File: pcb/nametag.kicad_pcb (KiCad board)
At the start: 2 copper layers, 80 x 55 mm, 34 parts, among them J1 Conn_01x04, SW1 TS02-66-43-BK-160-LCR-D, U2 AVR16DD20-I/SO, U3 TPS613226ADBVR

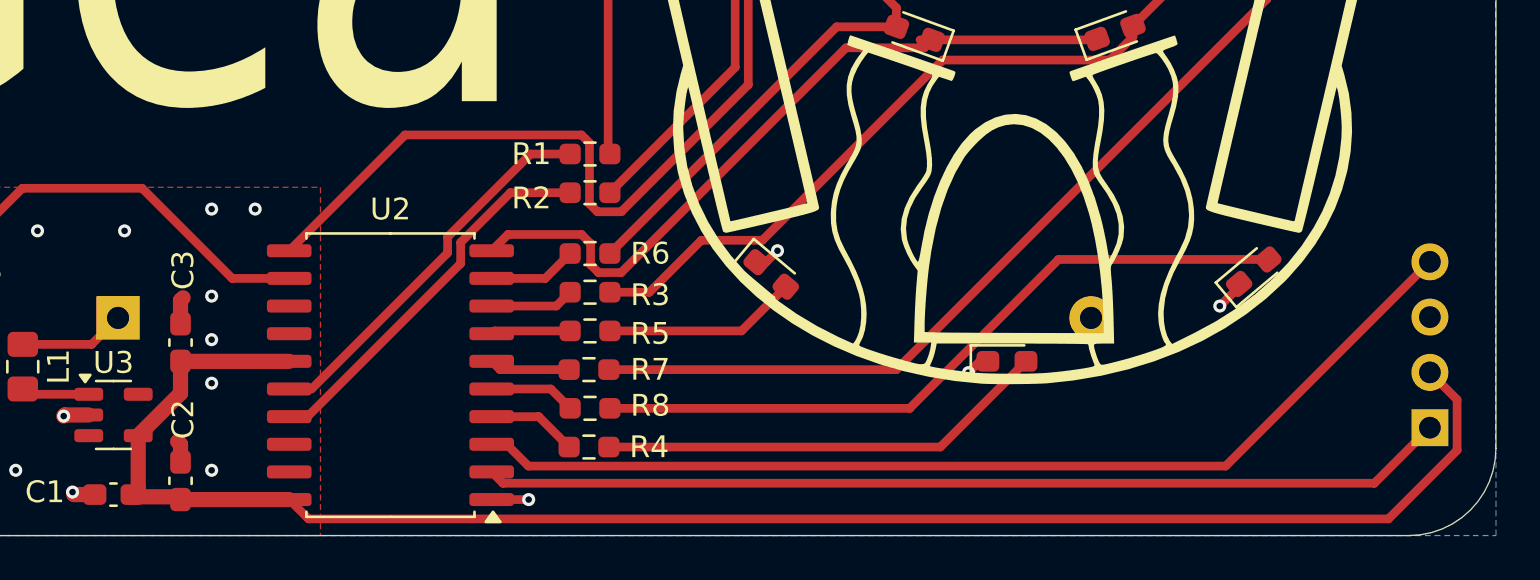
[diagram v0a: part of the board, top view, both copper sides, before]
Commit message: Swap to STC8H1K08 and work on JLCPCB assembly support
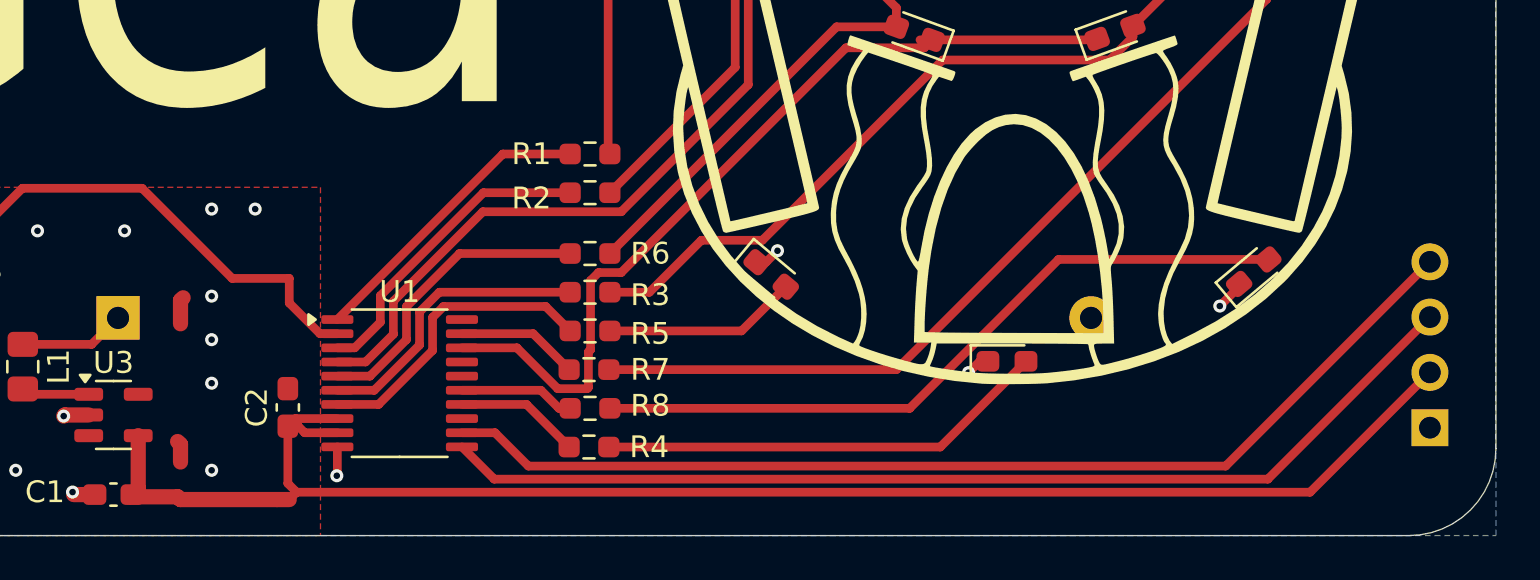
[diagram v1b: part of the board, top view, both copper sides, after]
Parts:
- removed C3: 0.1u, Capacitor_SMD:C_0603_1608Metric_Pad1.08x0.95mm_HandSolder
- removed U2: AVR16DD20-I/SO, Package_SO:SOIC-20W_7.5x12.8mm_P1.27mm
- added U1: ~, Package_SO:TSSOP-20_4.4x6.5mm_P0.65mm, F.Cu at (69.6, 88.0)
- C2: value 0.1u -> 100n
- moved C2 5.97 mm to (64.5, 89.1)
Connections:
- J1 pad 1: /Mcu/UPDI_RSTN -> GND
- J1 pad 3: GND -> /Mcu/UART_RX
- J1 pad 4: /Mcu/UPDI_PROG -> /Mcu/UART_TX
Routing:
- net /Mcu/UART_TX: track 0.00 -> 49.0 mm
- net /Mcu/UART_RX: track 0.00 -> 48.2 mm
- net /Mcu/UPDI_PROG: track 47.4 -> 0.00 mm
- net /Mcu/UPDI_RSTN: track 44.4 -> 0.00 mm
- net /Mcu/pwm3: track 3.66 -> 13.9 mm
- net /Mcu/pwm5: track 4.08 -> 13.9 mm
- net /Mcu/pwm4: track 3.87 -> 13.4 mm
- net +3.3V: track 79.0 -> 73.2 mm
- net /Mcu/cathode0: track 34.4 -> 40.0 mm
- net /Mcu/pwm6: track 17.8 -> 13.8 mm
- net /Mcu/switch: track 26.3 -> 30.3 mm
- net /Mcu/cathode1: track 61.5 -> 57.8 mm
- net /Mcu/pwm7: track 17.7 -> 14.4 mm
- net /Mcu/pwm2: track 3.72 -> 5.61 mm
- net /Mcu/pwm0: track 4.14 -> 5.73 mm
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
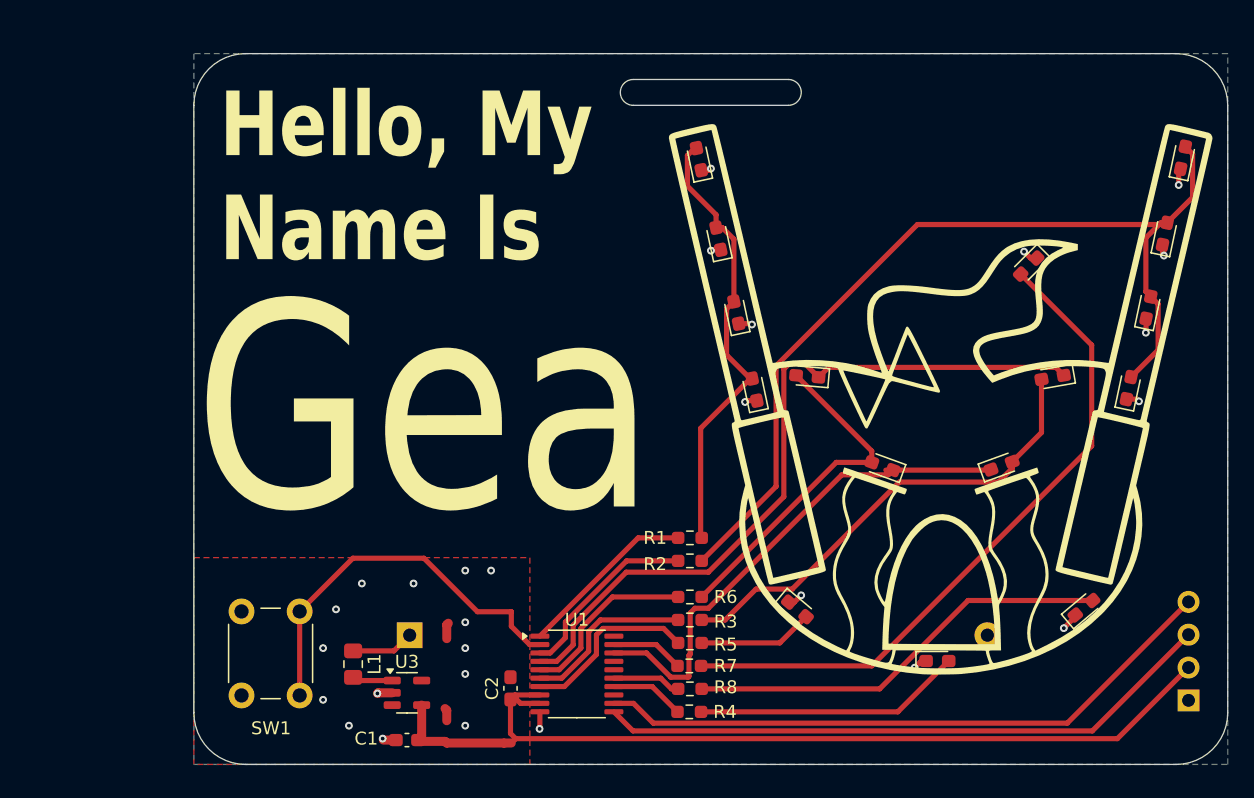
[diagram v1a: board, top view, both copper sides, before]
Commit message: More edits to PCB design
 - Change a couple of parts - voltage regulator - to use LCSC parts
 - Increase width of the nametag PCB
 - redo layout a bit
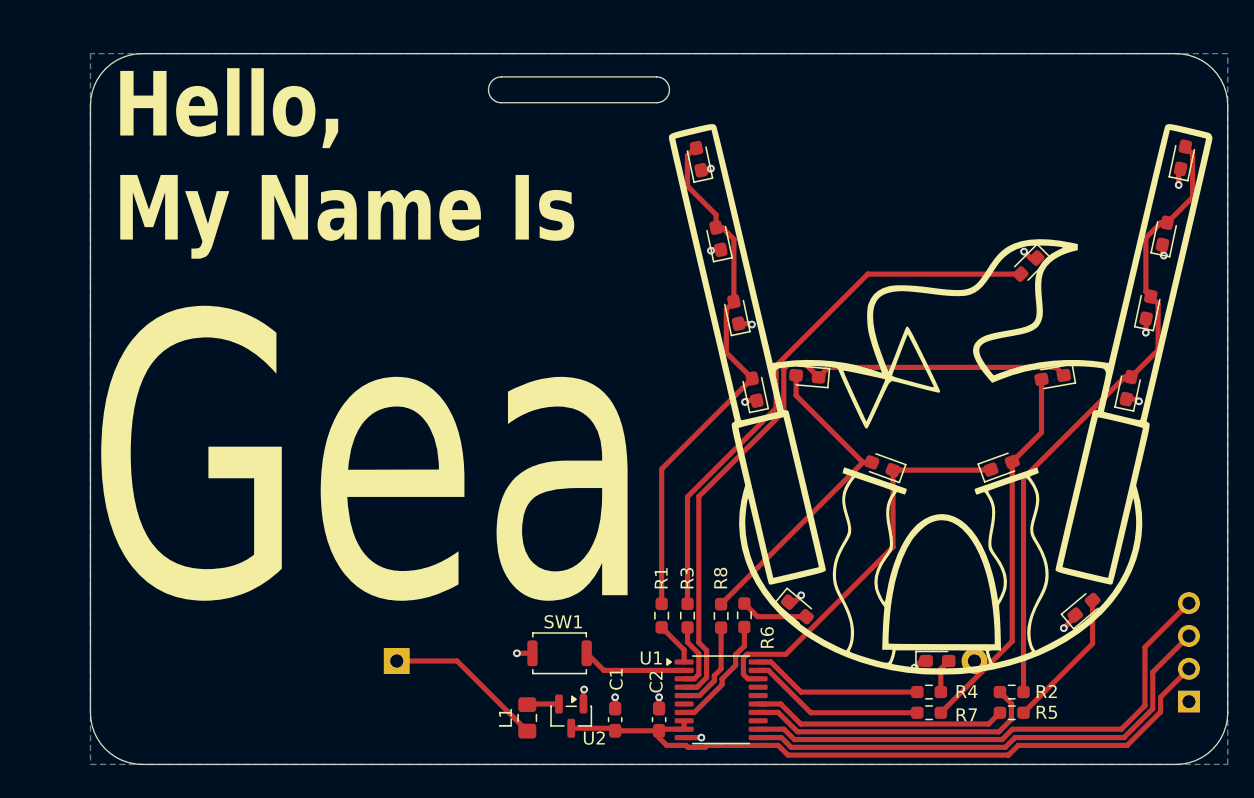
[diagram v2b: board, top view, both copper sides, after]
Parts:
- removed U3: TPS613226ADBVR, Package_TO_SOT_SMD:SOT-23-5
- added U2: BL8536CB3TR36, Package_TO_SOT_SMD:SOT-23, F.Cu at (69.2, 91.3)
- BT1: value Keystone Electronics 2466 -> C5290189
- SW1: value TS02-66-43-BK-160-LCR-D -> TS-1088-AR02016; footprint Button_Switch_THT:SW_PUSH_6mm_H4.3mm -> Button_Switch_SMD:SW_Push_SPST_NO_Alps_SKRK
- U1: value ~ -> STC8H1K08-TSSOP20
- moved R2 26.9 mm to (103.3, 89.4)
- moved R5 25.5 mm to (103.3, 91.0)
- moved SW1 20.4 mm to (68.3, 86.4), turned to 180 degrees
- moved R7 18.9 mm to (96.9, 91.0)
- moved R4 18.6 mm to (96.9, 89.4)
- moved C1 16.2 mm to (72.6, 91.5), turned to 90 degrees
- moved L1 14.1 mm to (65.8, 91.4), turned to 90 degrees
- moved C2 11.8 mm to (76.0, 91.5)
- moved U1 11.3 mm to (80.8, 90.0)
- moved R1 6.40 mm to (76.2, 83.5), turned to 90 degrees
- moved R8 6.14 mm to (80.8, 83.5), turned to 90 degrees
- moved R6 4.45 mm to (82.6, 83.5), turned to 90 degrees
- moved BT1 2.24 mm to (55.7, 87.0)
- moved R3 0.38 mm to (78.2, 83.5), turned to 90 degrees
- moved J1 0.10 mm to (117.0, 90.1)
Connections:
- R3 pad 1: /Mcu/pwm4 -> /Mcu/pwm2
- R3 pad 2: Net-(D11-A) -> Net-(D9-A)
- R5 pad 1: /Mcu/pwm3 -> /Mcu/pwm1
- R5 pad 2: Net-(D14-A) -> Net-(D13-A)
- R6 pad 1: /Mcu/pwm5 -> /Mcu/pwm3
- R6 pad 2: Net-(D12-A) -> Net-(D14-A)
- R7 pad 1: /Mcu/pwm2 -> /Mcu/pwm4
- R7 pad 2: Net-(D9-A) -> Net-(D11-A)
- R8 pad 1: /Mcu/pwm1 -> /Mcu/pwm5
- R8 pad 2: Net-(D13-A) -> Net-(D12-A)
- U1 pad 14: /Mcu/pwm0 -> /Mcu/pwm7
- U1 pad 19: /Mcu/pwm2 -> /Mcu/pwm4
- U1 pad 20: unconnected-(U1-P1.1/ADC1/TxD2/PWM1N-Pad20) -> /Mcu/pwm0
- U1 pad 3: /Mcu/pwm7 -> /Mcu/pwm2
- U1 pad 6: /Mcu/pwm4 -> unconnected-(U1-P1.7/TxD_3/XTALI/PWM5_2/PWM4N-Pad6)
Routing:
- net Net-(D5-A): track 72.7 -> 49.2 mm
- net Net-(D13-A): track 33.1 -> 10.9 mm
- net /Mcu/switch: track 30.3 -> 8.09 mm
- net Net-(D10-A): track 20.8 -> 2.66 mm
- net +3.3V: track 73.2 -> 55.2 mm
- net /Mcu/pwm1: track 5.31 -> 19.7 mm
- net /Mcu/pwm6: track 13.8 -> 3.39 mm
- net Net-(D9-A): track 52.9 -> 43.1 mm
- net /Mcu/UART_RX: track 48.2 -> 38.9 mm
- net /Mcu/cathode0: track 40.0 -> 31.2 mm
- net /Mcu/pwm7: track 14.4 -> 23.1 mm
- net /Mcu/UART_TX: track 49.0 -> 40.7 mm
- net Net-(D11-A): track 36.7 -> 29.0 mm
- net /Mcu/pwm0: track 5.73 -> 13.3 mm
- net Net-(BT1-+): track 4.88 -> 12.3 mm
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- removed copper zone on F.Cu, net GND
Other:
- board size 80 x 55 mm -> 88 x 55 mm

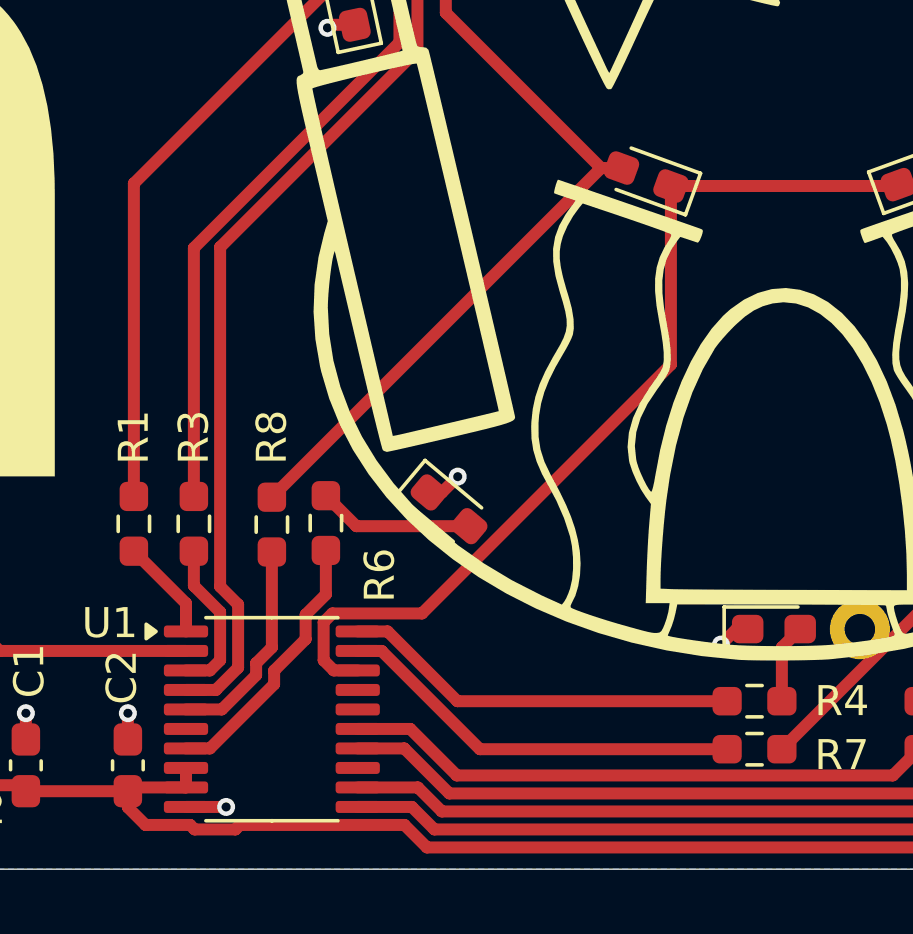
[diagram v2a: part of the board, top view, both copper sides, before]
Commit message: Update PCB to reflect PWM pin assignments
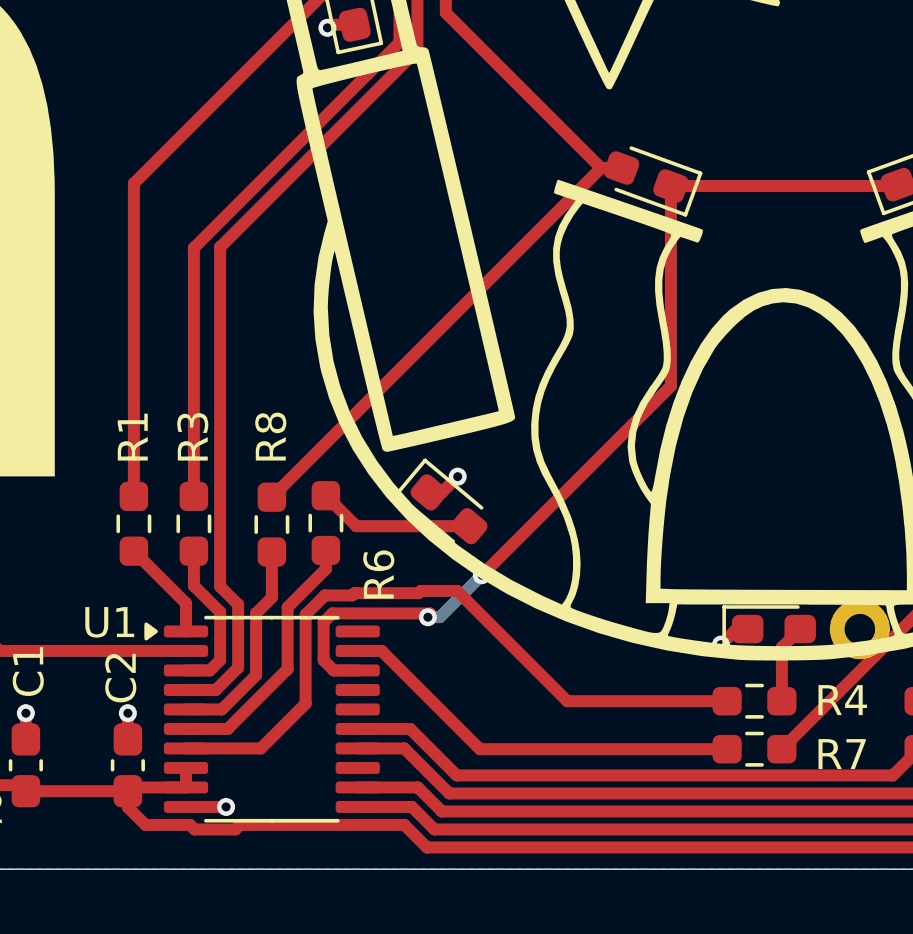
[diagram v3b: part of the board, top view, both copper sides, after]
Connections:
- U1 pad 20: /Mcu/pwm0 -> unconnected-(U1-P1.1/ADC1/TxD2/PWM1N-Pad20)
- U1 pad 6: unconnected-(U1-P1.7/TxD_3/XTALI/PWM5_2/PWM4N-Pad6) -> /Mcu/pwm3
- U1 pad 7: /Mcu/pwm3 -> /Mcu/pwm0
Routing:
- net /Mcu/pwm0: track 13.3 -> 23.5 mm
- net /Mcu/cathode0: track 31.2 -> 31.9 mm, vias 0 -> 2

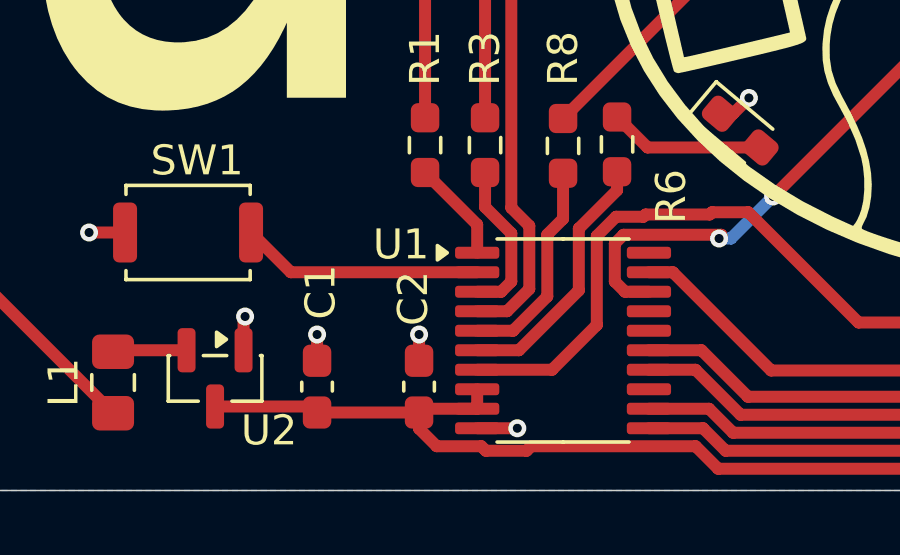
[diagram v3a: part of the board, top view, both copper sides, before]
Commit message: Update PCB with new naming of PWM channels
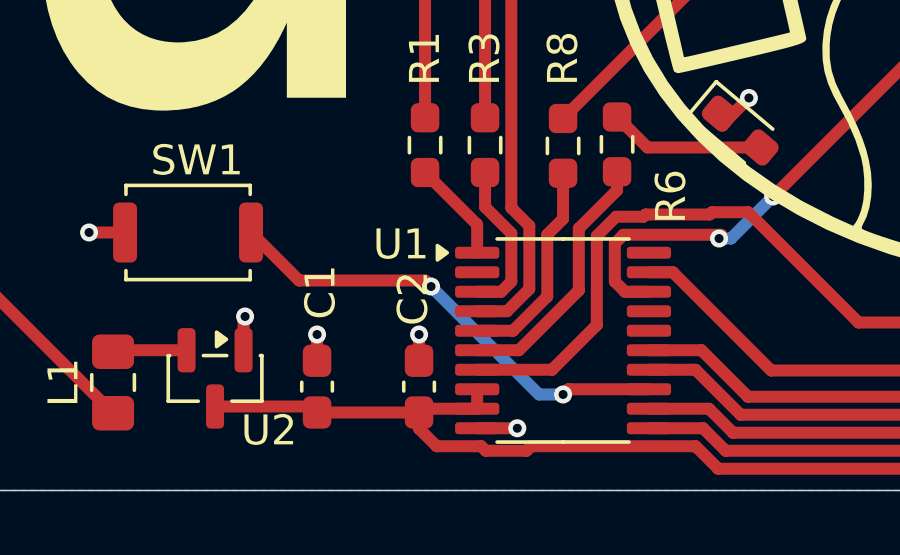
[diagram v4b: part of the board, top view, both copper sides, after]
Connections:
- R1 pad 1: /Mcu/pwm6 -> /Mcu/pwm2
- R3 pad 1: /Mcu/pwm2 -> /Mcu/pwm3
- R4 pad 1: /Mcu/pwm0 -> /Mcu/pwm6
- R5 pad 1: /Mcu/pwm1 -> /Mcu/pwm8
- R6 pad 1: /Mcu/pwm3 -> /Mcu/pwm5
- R7 pad 1: /Mcu/pwm4 -> /Mcu/pwm1
- R8 pad 1: /Mcu/pwm5 -> /Mcu/pwm4
- U1 pad 1: /Mcu/pwm6 -> /Mcu/pwm2
- U1 pad 13: unconnected-(U1-PWMETI/PWMETI2/INT0/SCLK_4/I2CSCL_4/ADC10/P3.2-Pad13) -> /Mcu/switch
- U1 pad 15: /Mcu/pwm1 -> /Mcu/pwm8
- U1 pad 19: /Mcu/pwm4 -> /Mcu/pwm1
- U1 pad 2: /Mcu/switch -> unconnected-(U1-P1.3/MOSI/T2CLKO/PWM2N-Pad2)
- U1 pad 3: /Mcu/pwm2 -> /Mcu/pwm3
- U1 pad 5: /Mcu/pwm5 -> /Mcu/pwm4
- U1 pad 6: /Mcu/pwm3 -> /Mcu/pwm5
- U1 pad 7: /Mcu/pwm0 -> /Mcu/pwm6
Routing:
- net /Mcu/pwm0: track 23.5 -> 0.00 mm
- net /Mcu/pwm6: track 3.39 -> 23.5 mm
- net /Mcu/pwm8: track 0.00 -> 19.7 mm
- net /Mcu/switch: track 8.09 -> 15.6 mm, vias 0 -> 2
- net /Mcu/pwm4: track 13.7 -> 7.19 mm
- net /Mcu/pwm1: track 19.7 -> 13.7 mm
- net /Mcu/pwm3: track 8.70 -> 5.28 mm
- net /Mcu/pwm2: track 5.28 -> 3.39 mm
- net /Mcu/pwm5: track 7.19 -> 8.70 mm

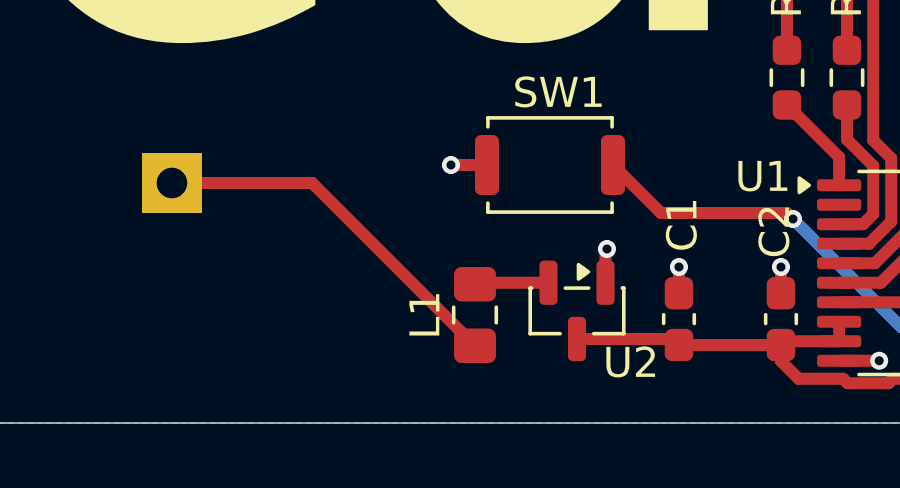
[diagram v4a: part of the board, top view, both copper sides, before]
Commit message: Small changes for manufacturability
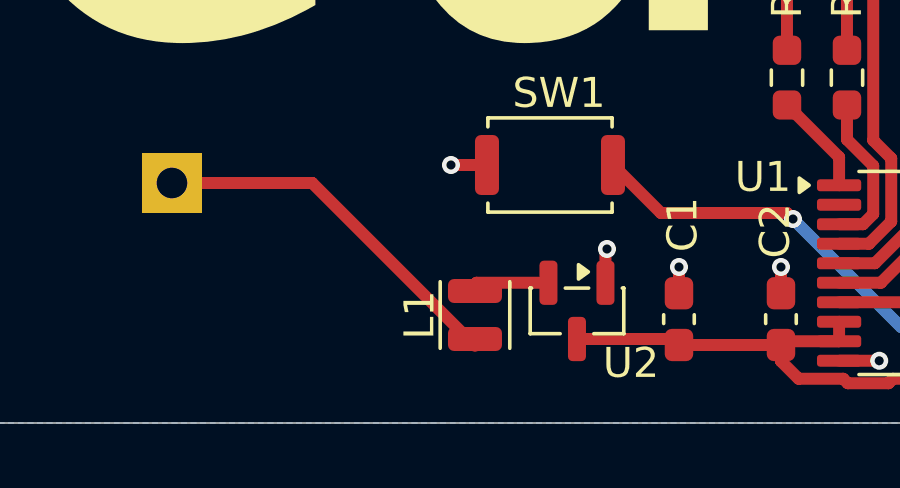
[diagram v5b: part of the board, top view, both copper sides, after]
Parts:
- L1: footprint Inductor_SMD:L_0805_2012Metric_Pad1.15x1.40mm_HandSolder -> Inductor_SMD:L_Wuerth_PMFI-201610_PMCI-compatible
